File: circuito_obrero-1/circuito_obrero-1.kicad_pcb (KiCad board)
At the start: 2 copper layers, 49 parts, among them J1 Conn_01x03_Pin, J10 Conn_01x05, J2 Conn_01x03_Pin, J3 Conn_01x03_Pin, J4 Conn_01x03_Pin, J5 Conn_01x03_Pin, J6 Conn_01x03_Pin, J7 Conn_01x03_Pin, J8 Conn_01x03_Pin, J9 Conn_01x05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

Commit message: probando rerutear
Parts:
- moved H_B_j3_pin3 50.1 mm to (89.0, 115.0), turned to 90 degrees
- moved J3 39.0 mm to (96.0, 111.0), turned to -90 degrees
- moved R8 29.4 mm to (89.2, 98.0), turned to 0 degrees
- moved R7 28.8 mm to (90.0, 103.2), turned to -90 degrees
- moved H3_B_j8_pin1 22.6 mm to (174.0, 93.0)
- moved R6 21.1 mm to (83.0, 104.2)
- moved R4 15.5 mm to (75.0, 96.4)
- moved R5 14.4 mm to (87.0, 101.2)
- moved J2 11.9 mm to (79.0, 106.0), turned to -90 degrees
- moved H_A_j3_pin3 8.73 mm to (109.0, 70.0)
- moved H4_GND1 8.51 mm to (87.0, 92.0)
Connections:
- H3_B_j8_pin1 pad 1: Net-(H3_B_j8_pin1-Pad1) -> Net-(J8-Pin_1)
- H_A_j3_pin3 pad 1: Net-(H_A_j3_pin3-Pad1) -> Net-(J3-Pin_3)
- R16 pad 1: Net-(H3_B_j8_pin1-Pad1) -> Net-(J8-Pin_1)
- R9 pad 1: Net-(H_A_j3_pin3-Pad1) -> Net-(J3-Pin_3)
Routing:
- net Net-(J10-Pin_2): track 172.6 -> 128.3 mm
- net Net-(J9-Pin_3): track 62.7 -> 103.7 mm
- net Net-(J2-Pin_1): track 41.8 -> 79.2 mm
- net GND: track 202.5 -> 170.0 mm
- net Net-(J10-Pin_1): track 150.2 -> 118.3 mm
- net Net-(J2-Pin_3): track 11.5 -> 34.6 mm
- net Net-(J2-Pin_2): track 16.2 -> 35.5 mm
- net Net-(J10-Pin_3): track 69.6 -> 88.5 mm
- net Net-(J3-Pin_2): track 33.5 -> 21.4 mm
- net Net-(H3_B_j8_pin1-Pad1): track 11.8 -> 0.00 mm
- net Net-(J8-Pin_1): track 19.2 -> 31.0 mm
- net VCC: track 215.3 -> 204.7 mm
- net Net-(H_A_j3_pin3-Pad1): track 9.27 -> 0.00 mm
- net Net-(J3-Pin_3): track 30.5 -> 34.8 mm
- net Net-(J3-Pin_1): track 27.4 -> 28.6 mm

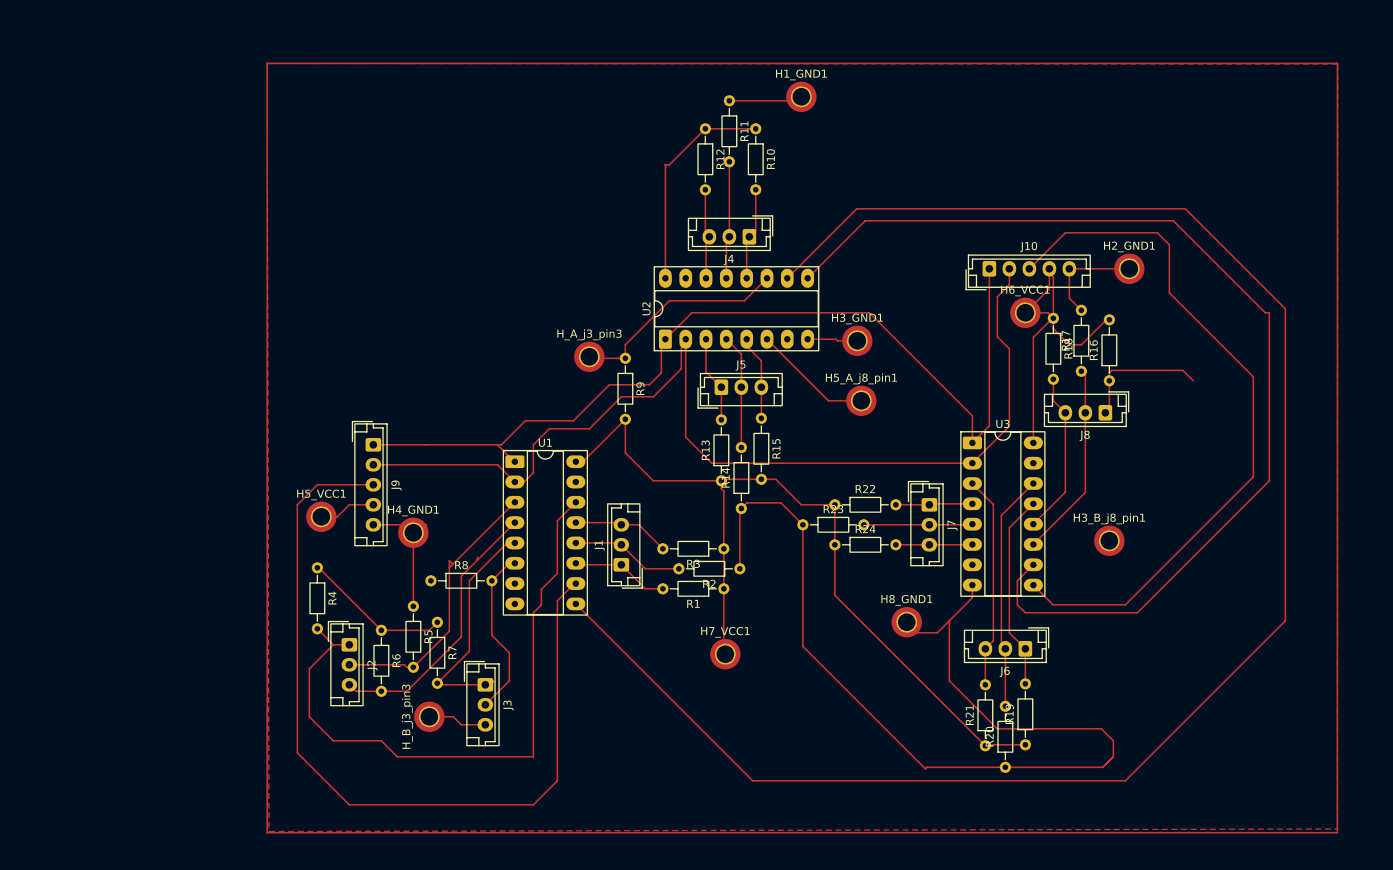
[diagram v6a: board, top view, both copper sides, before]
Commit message: recableando mas prolijo
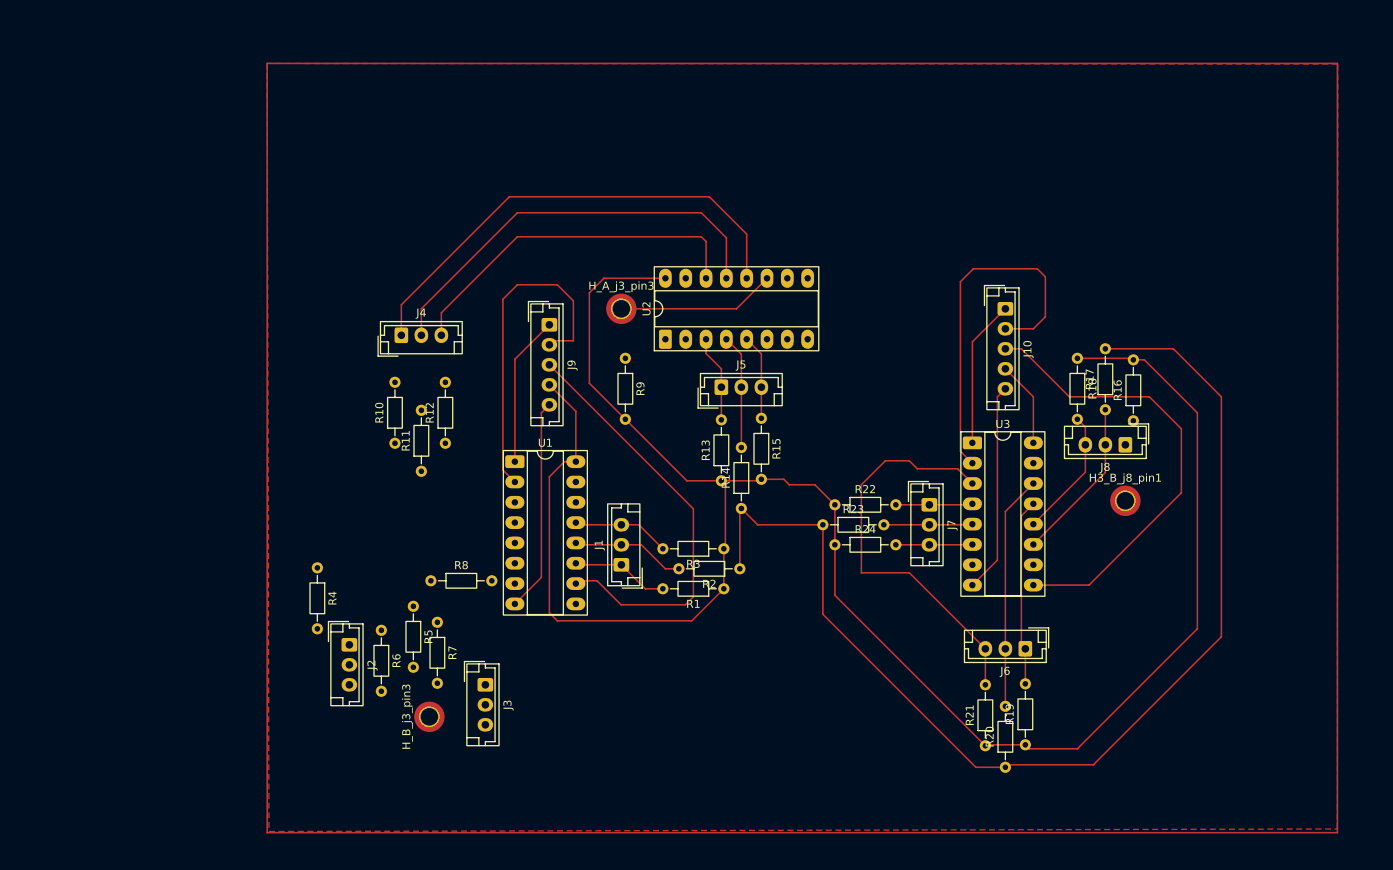
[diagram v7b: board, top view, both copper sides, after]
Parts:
- removed H1_GND1, H2_GND1, H3_GND1, H4_GND1, H5_A_j8_pin1, H5_VCC1, H6_VCC1, H7_VCC1, H8_GND1: MountingHole_Pad, MountingHole:MountingHole_2.2mm_M2_DIN965_Pad_TopOnly
- moved R11 60.2 mm to (88.0, 84.3), turned to 90 degrees
- moved R10 59.8 mm to (84.7, 80.8), turned to 90 degrees
- moved R12 51.0 mm to (91.0, 80.8), turned to 90 degrees
- moved J4 45.2 mm to (85.5, 67.3), turned to 0 degrees
- moved J9 26.6 mm to (104.0, 66.0)
- moved H_A_j3_pin3 7.21 mm to (113.0, 64.0)
- moved R16 5.83 mm to (177.0, 78.0)
- moved R18 5.83 mm to (170.0, 70.2)
- moved R17 5.67 mm to (173.5, 76.6)
- moved H3_B_j8_pin1 5.39 mm to (176.0, 88.0)
- moved J10 5.39 mm to (161.0, 64.0), turned to -90 degrees
- moved J8 4.72 mm to (176.0, 81.0)
- moved R23 2.50 mm to (138.2, 91.0)
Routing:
- net Net-(U1-Q7): track 216.2 -> 0.00 mm
- net Net-(U2-Q7): track 131.0 -> 0.00 mm
- net Net-(J10-Pin_1): track 118.3 -> 37.4 mm
- net Net-(J2-Pin_1): track 79.2 -> 0.00 mm
- net Net-(J9-Pin_3): track 103.7 -> 52.9 mm
- net VCC: track 204.7 -> 254.9 mm
- net Net-(J4-Pin_1): track 11.6 -> 60.0 mm
- net Net-(J10-Pin_2): track 128.3 -> 87.7 mm
- net Net-(J4-Pin_2): track 15.0 -> 52.8 mm
- net Net-(J2-Pin_2): track 35.5 -> 0.00 mm
- net Net-(J2-Pin_3): track 34.6 -> 0.00 mm
- net Net-(J4-Pin_3): track 11.5 -> 44.7 mm
- net Net-(J10-Pin_3): track 88.5 -> 57.4 mm
- net Net-(J8-Pin_1): track 31.0 -> 0.00 mm
- net Net-(J3-Pin_1): track 28.6 -> 0.00 mm
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
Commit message: pre añadir lagrimas
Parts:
- removed H_A_j3_pin3, H_B_j3_pin3: MountingHole_Pad, MountingHole:MountingHole_2.2mm_M2_DIN965_Pad_TopOnly
- added H5_A_j8_pin1: MountingHole_Pad, MountingHole:MountingHole_2.2mm_M2_DIN965_Pad_TopOnly, F.Cu at (148.0, 68.0)
- added PUENTE_1: 0k, Resistor_THT:R_Axial_DIN0204_L3.6mm_D1.6mm_P7.62mm_Horizontal, F.Cu at (123.1, 64.0)
- added PUENTE_2: 0k, Resistor_THT:R_Axial_DIN0204_L3.6mm_D1.6mm_P7.62mm_Horizontal, F.Cu at (118.0, 53.1)
- added PUENTE_3: 0k, Resistor_THT:R_Axial_DIN0204_L3.6mm_D1.6mm_P7.62mm_Horizontal, F.Cu at (120.0, 92.2)
- added PUENTE_4: 0k, Resistor_THT:R_Axial_DIN0204_L3.6mm_D1.6mm_P7.62mm_Horizontal, F.Cu at (154.0, 55.0)
- added PUENTE_5: 0k, Resistor_THT:R_Axial_DIN0207_L6.3mm_D2.5mm_P15.24mm_Horizontal, F.Cu at (202.6, 76.0)
- added PUENTE_6: 0k, Resistor_THT:R_Axial_DIN0207_L6.3mm_D2.5mm_P10.16mm_Horizontal, F.Cu at (106.0, 106.2)
- added PUENTE_7: 0k, Resistor_THT:R_Axial_DIN0204_L3.6mm_D1.6mm_P7.62mm_Horizontal, F.Cu at (172.0, 56.6)
- added PUENTE_8: 0k, Resistor_THT:R_Axial_DIN0207_L6.3mm_D2.5mm_P10.16mm_Horizontal, F.Cu at (142.0, 97.0)
- added PUENTE_9: 0k, Resistor_THT:R_Axial_DIN0204_L3.6mm_D1.6mm_P7.62mm_Horizontal, F.Cu at (176.0, 52.0)
- moved J2 41.2 mm to (103.0, 72.5)
- moved R20 33.4 mm to (149.8, 89.9), turned to 0 degrees
- moved R21 32.0 mm to (151.7, 87.4), turned to 0 degrees
- moved R4 28.7 mm to (90.2, 72.0), turned to 0 degrees
- moved R19 28.6 mm to (151.8, 92.4), turned to 0 degrees
- moved R6 27.2 mm to (90.2, 78.0), turned to 0 degrees
- moved J3 26.9 mm to (103.0, 85.0)
- moved R5 26.2 mm to (88.2, 75.0), turned to 0 degrees
- moved R9 25.5 mm to (98.8, 91.0), turned to 180 degrees
- moved R11 23.6 mm to (79.1, 62.5), turned to 0 degrees
- moved R10 21.8 mm to (81.7, 59.2), turned to 0 degrees
- moved H3_B_j8_pin1 20.2 mm to (187.6, 71.5)
- moved J6 19.4 mm to (175.1, 91.0)
- moved J7 19.4 mm to (163.1, 73.0)
- moved R16 19.4 mm to (188.6, 62.5)
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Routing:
- net VCC: track 254.9 -> 556.6 mm
- net GND: track 194.2 -> 392.7 mm
- net Net-(U1-Q7): track 0.00 -> 191.5 mm
- net Net-(U2-Q7): track 0.00 -> 113.4 mm
- net Net-(J3-Pin_3): track 19.8 -> 131.3 mm
- net Net-(J2-Pin_1): track 0.00 -> 79.2 mm
- net Net-(J10-Pin_2): track 87.7 -> 157.7 mm
- net Net-(J8-Pin_1): track 0.00 -> 57.5 mm
- net Net-(J10-Pin_1): track 37.4 -> 94.7 mm
- net Net-(J4-Pin_3): track 44.7 -> 69.6 mm
- net Net-(J4-Pin_2): track 52.8 -> 74.2 mm
- net Net-(J6-Pin_1): track 23.3 -> 41.0 mm
- net Net-(J4-Pin_1): track 60.0 -> 74.2 mm
- net Net-(J3-Pin_2): track 0.00 -> 13.9 mm
- net Net-(J2-Pin_2): track 0.00 -> 13.6 mm
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- removed copper zone on F.Cu, net GND
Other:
- board outline added: 138.6 x 79.1 mm
